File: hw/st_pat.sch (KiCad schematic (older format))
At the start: 16 parts

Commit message: Switch to use Feather M0 Adalogger board
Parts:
- removed C? (x2): 1uF, symbol Device:C_Small
- removed C?: 10uF, symbol Device:C_Small
- removed D?: LED, symbol Device:LED
- removed D?: MBR120, symbol Device:D
- removed J?: USB_B, symbol Connector:USB_B
- removed J?: BATTERY, symbol Connector:Conn_01x02_Female
- removed J?: Micro_SD_Card, symbol Connector:Micro_SD_Card
- removed Q?: DMG3415U, Package_TO_SOT_SMD:SOT-23, symbol Transistor_FET:DMG3414U
- removed R?: 10K, symbol Device:R_US
- removed R?: 1K, symbol Device:R_US
- removed R?: 100K, symbol Device:R_US
- removed U?: ATSAMD51J19A-A, Package_QFP:TQFP-64_10x10mm_P0.5mm, symbol MCU_Microchip_SAMD:ATSAMD51J19A-A
- removed U?: MCP73831-2-OT, Package_TO_SOT_SMD:SOT-23-5, symbol Battery_Management:MCP73831-2-OT
- removed U?: AP2112K-3.3, Package_TO_SOT_SMD:SOT-23-5, symbol Regulator_Linear:AP2112K-3.3
- added J1: Feather Left, symbol Connector:Conn_01x16_Female
- added J2: Feather Right, symbol Connector:Conn_01x12_Female
- added J3: Conn_01x09_Female, symbol Connector:Conn_01x09_Female
- added J4: BATTERY, symbol Connector:Conn_01x02_Female
- added SW1: SW_MEC_5G, symbol Switch:SW_MEC_5G
- gave numbers to parts that had none: 1
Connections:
- net labels added: +3V3, A0, A1, A2, A3, A4, A5, AREF, D10, D11, D12, D13, D5, D6, D7, D9, EN, MISO, MOSI, RST, RX, SCI, SCK, SDA, TX, VBAT
- net labels removed: +3.3V, D+, D-, SCLK, SD_CS, SD_MISO, SD_MOSI
- wire segments 33 -> 13
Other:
- note added: "FEATHER PINS"
- note added: "SHARP DISPLAY"
- note removed: "10K = 100mA\nMay change depending on battery"
- note removed: "I have no idea what capacitor values to use :P"
- moved on the sheet: U1

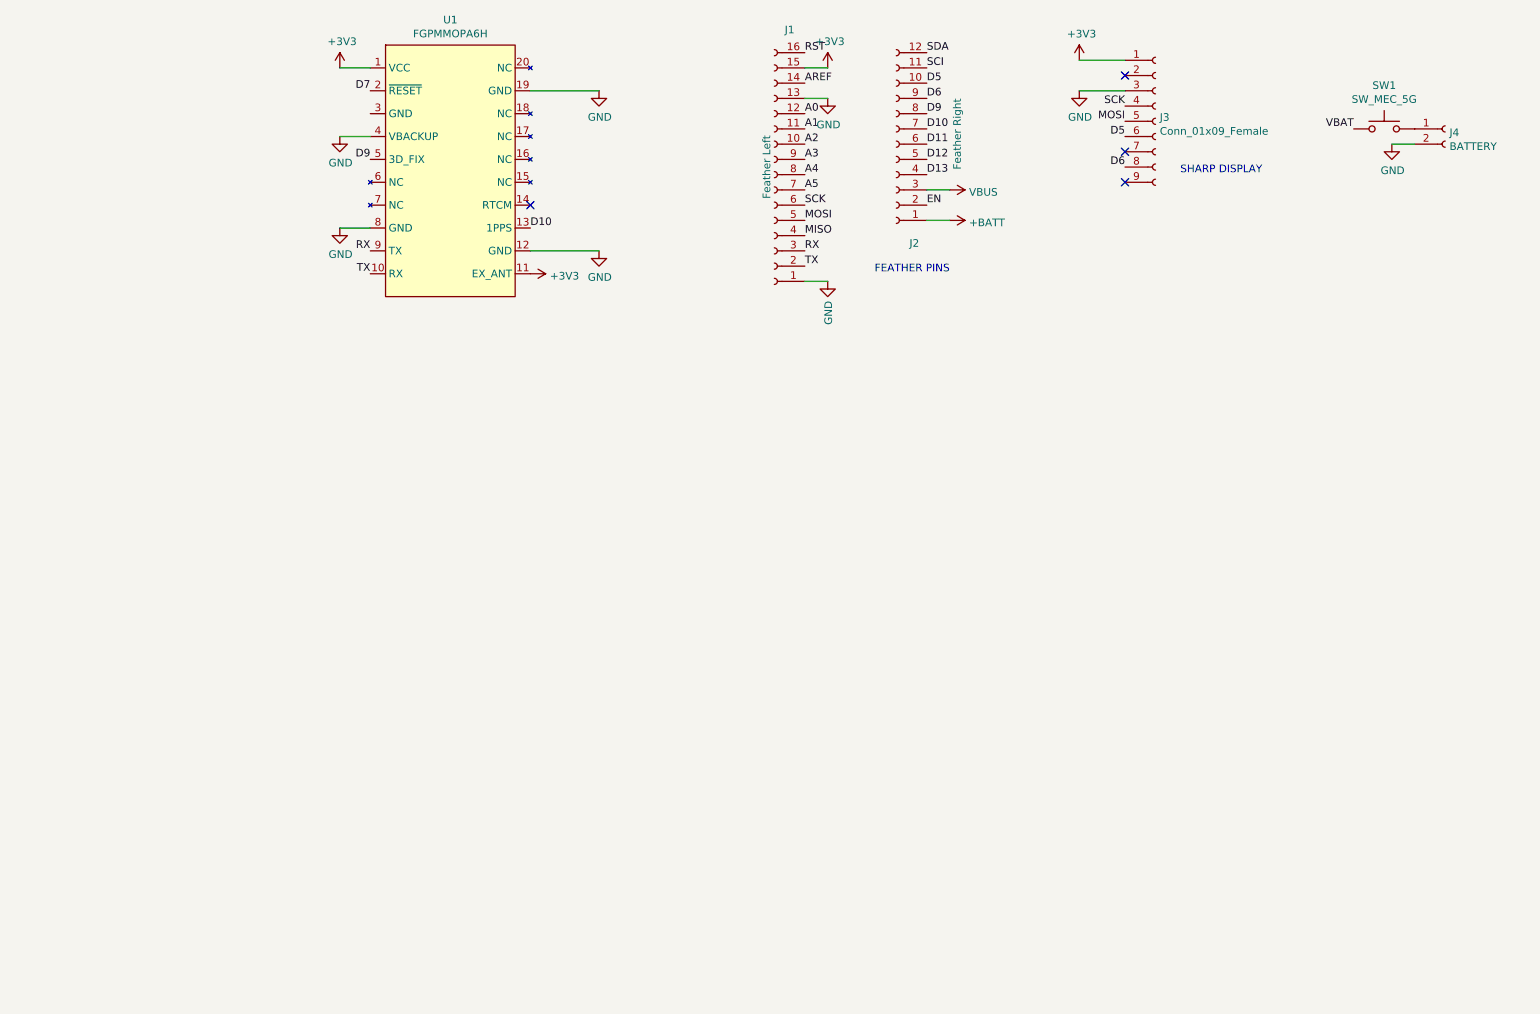
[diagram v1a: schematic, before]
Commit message: add compass to schematic
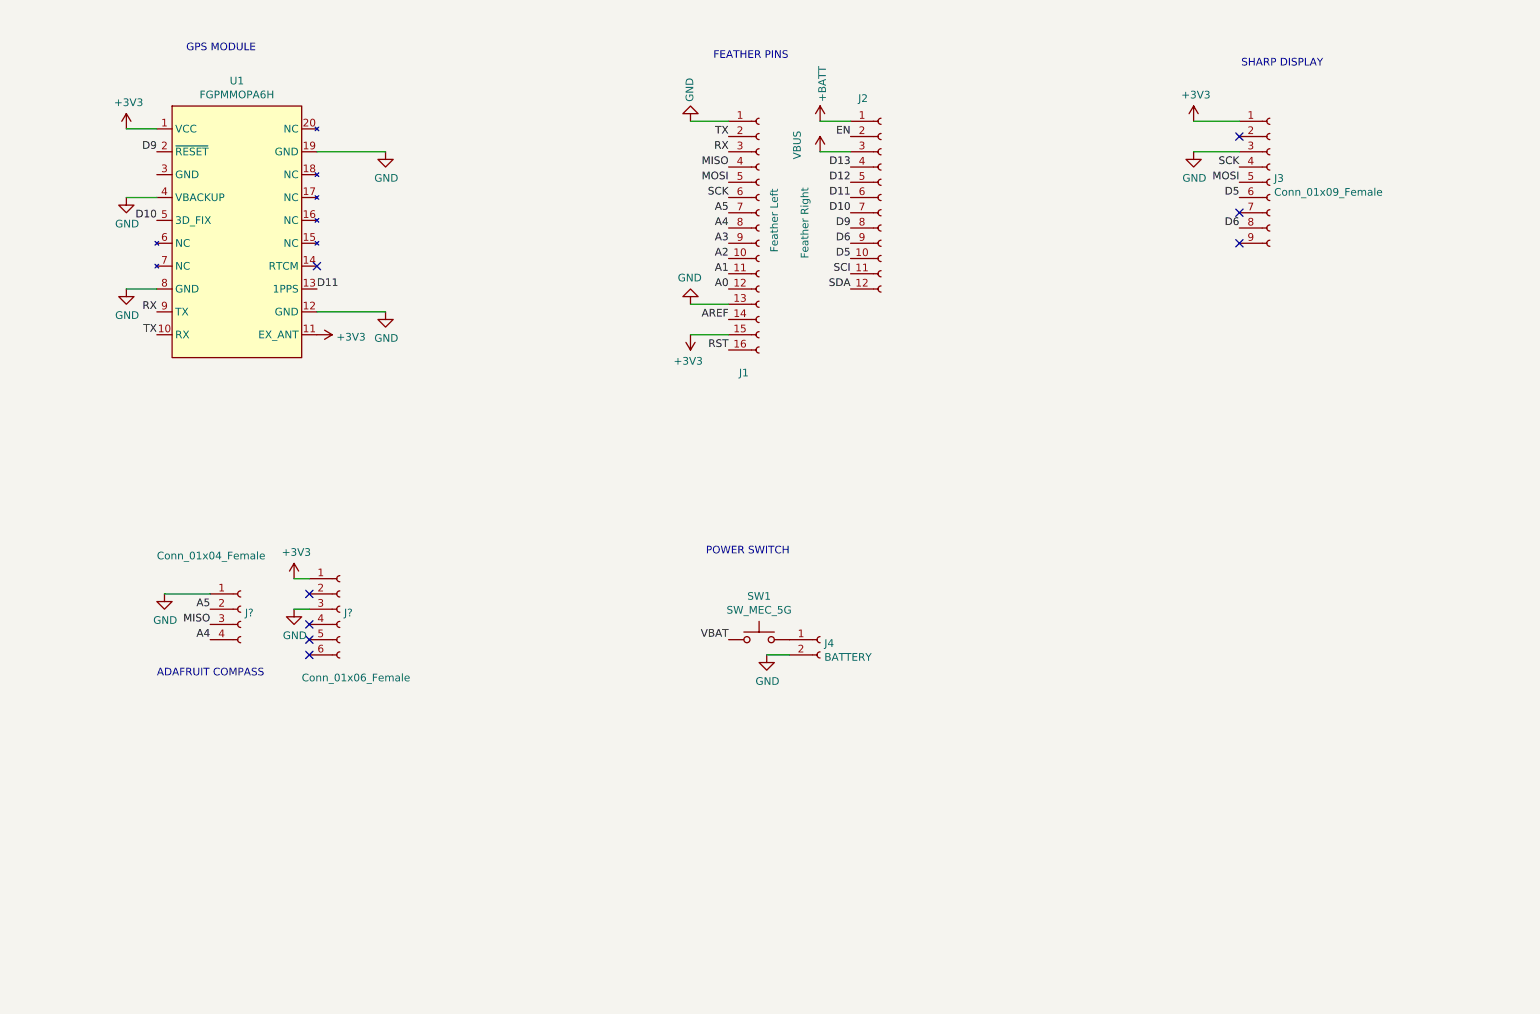
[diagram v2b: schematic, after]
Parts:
- added J?: Conn_01x04_Female, symbol Connector:Conn_01x04_Female
- added J?: Conn_01x06_Female, symbol Connector:Conn_01x06_Female
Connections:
- net D7 is gone; now on net D9: U1.2 (~RESET)
- net +3V3: now also J?.1 (Pin_1)
- net A4: now also J?.4 (Pin_4)
- net A5: now also J?.2 (Pin_2)
- net D10: now also U1.5 (3D_FIX); no longer U1.13 (1PPS)
- net D11: now also U1.13 (1PPS)
- net D9: no longer U1.5 (3D_FIX)
- net GND: now also J?.1 (Pin_1), J?.3 (Pin_3)
- net MISO: now also J?.3 (Pin_3)
- no-connect marks 4 -> 8
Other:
- note added: "ADAFRUIT COMPASS"
- note added: "GPS MODULE"
- note added: "POWER SWITCH"
- moved on the sheet: J1, J2, J3, J4, SW1, U1

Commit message: Update schematic - clearer label, add capacitor to GPS
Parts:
- added C1: 1uF, symbol Device:C_Small
- added C2: 0.01uF, symbol Device:C_Small
- added D1: LED, symbol Device:LED
- added R1: 330, symbol Device:R_US
- SW1: symbol Switch:SW_MEC_5G -> Switch:SW_SPST
- gave numbers to parts that had none: 2
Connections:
- net +3V3: now also C1.1, C2.1; no longer U1.11 (EX_ANT)
- net +BATT: now also SW1.1 (A)
- net GND: now also U1.3 (GND), C1.2, C2.2, R1.2; no longer U1.4 (VBACKUP)
- net SCK: now also J6.4 (Pin_4)
- net A4 renamed CPS_CS
- net A5 renamed CPS_RDY
- net D10 renamed GPS_FIX
- net GPS_FIX: now also D1.2 (A)
- net D11 renamed GPS_PPS
- net D5 renamed SHARP_CS
- net D6 renamed SHARP_DISP
- net D9 renamed GPS_RST
- net VBAT: no longer names the net of SW1.2 (B)
- net VBAT: now also J4.1 (Pin_1); no longer SW1.1 (A)
- new net: D1.1 (K), R1.1
- no-connect marks 8 -> 9
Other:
- moved on the sheet: J2, J6

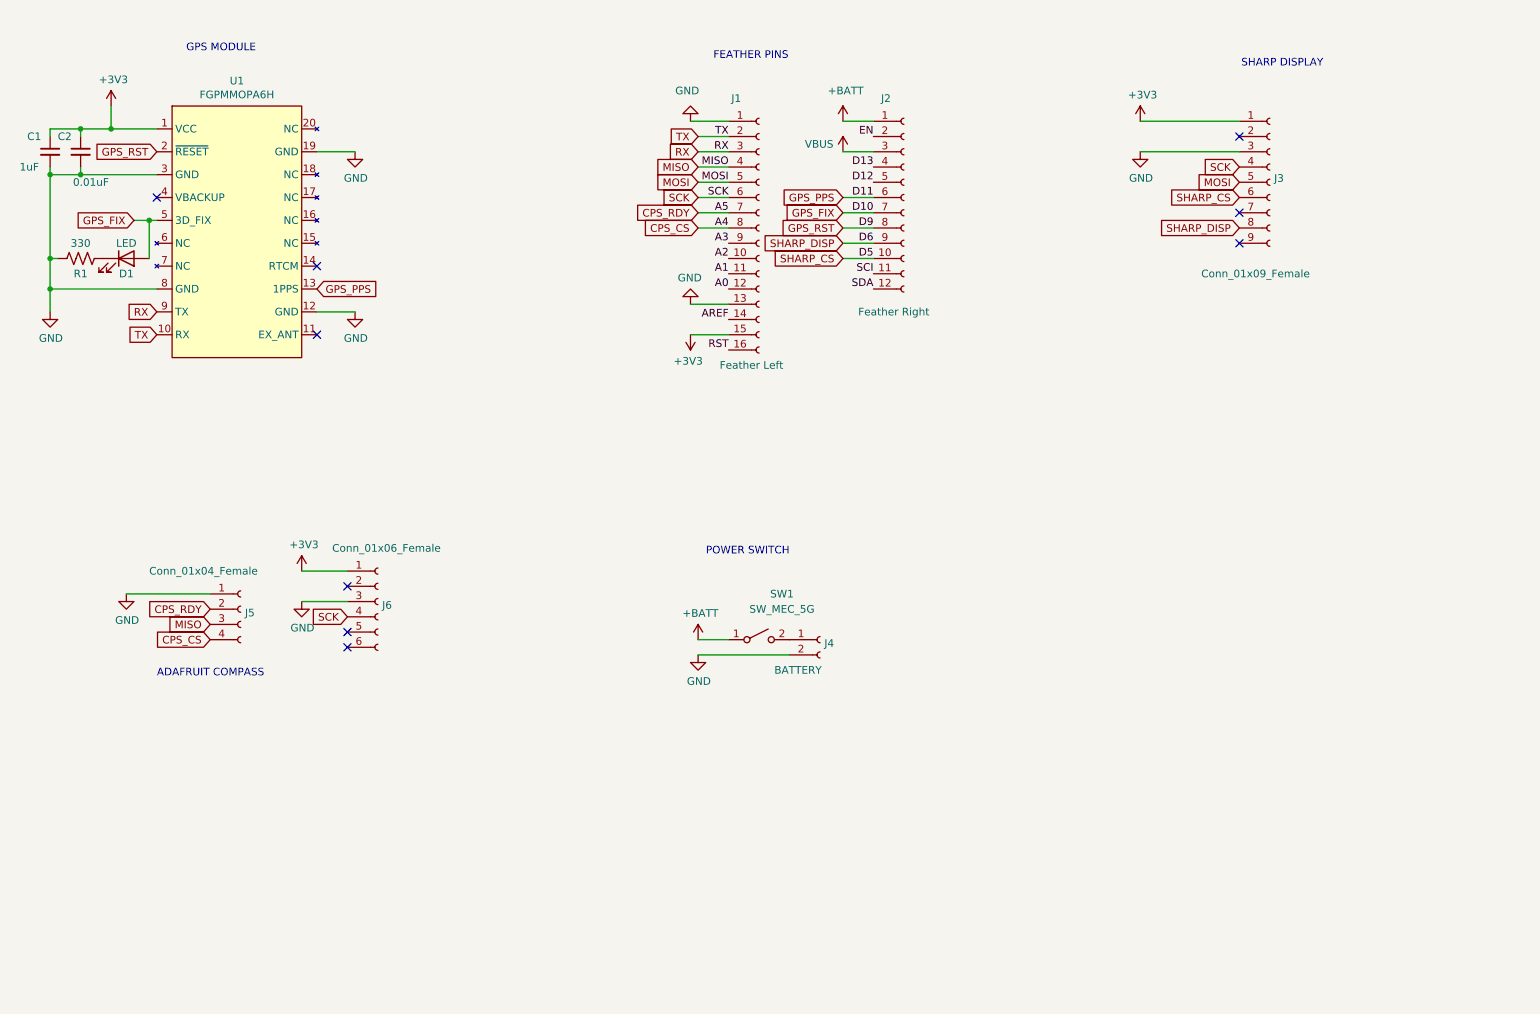
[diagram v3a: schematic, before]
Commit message: Remove global tags and fix ERC
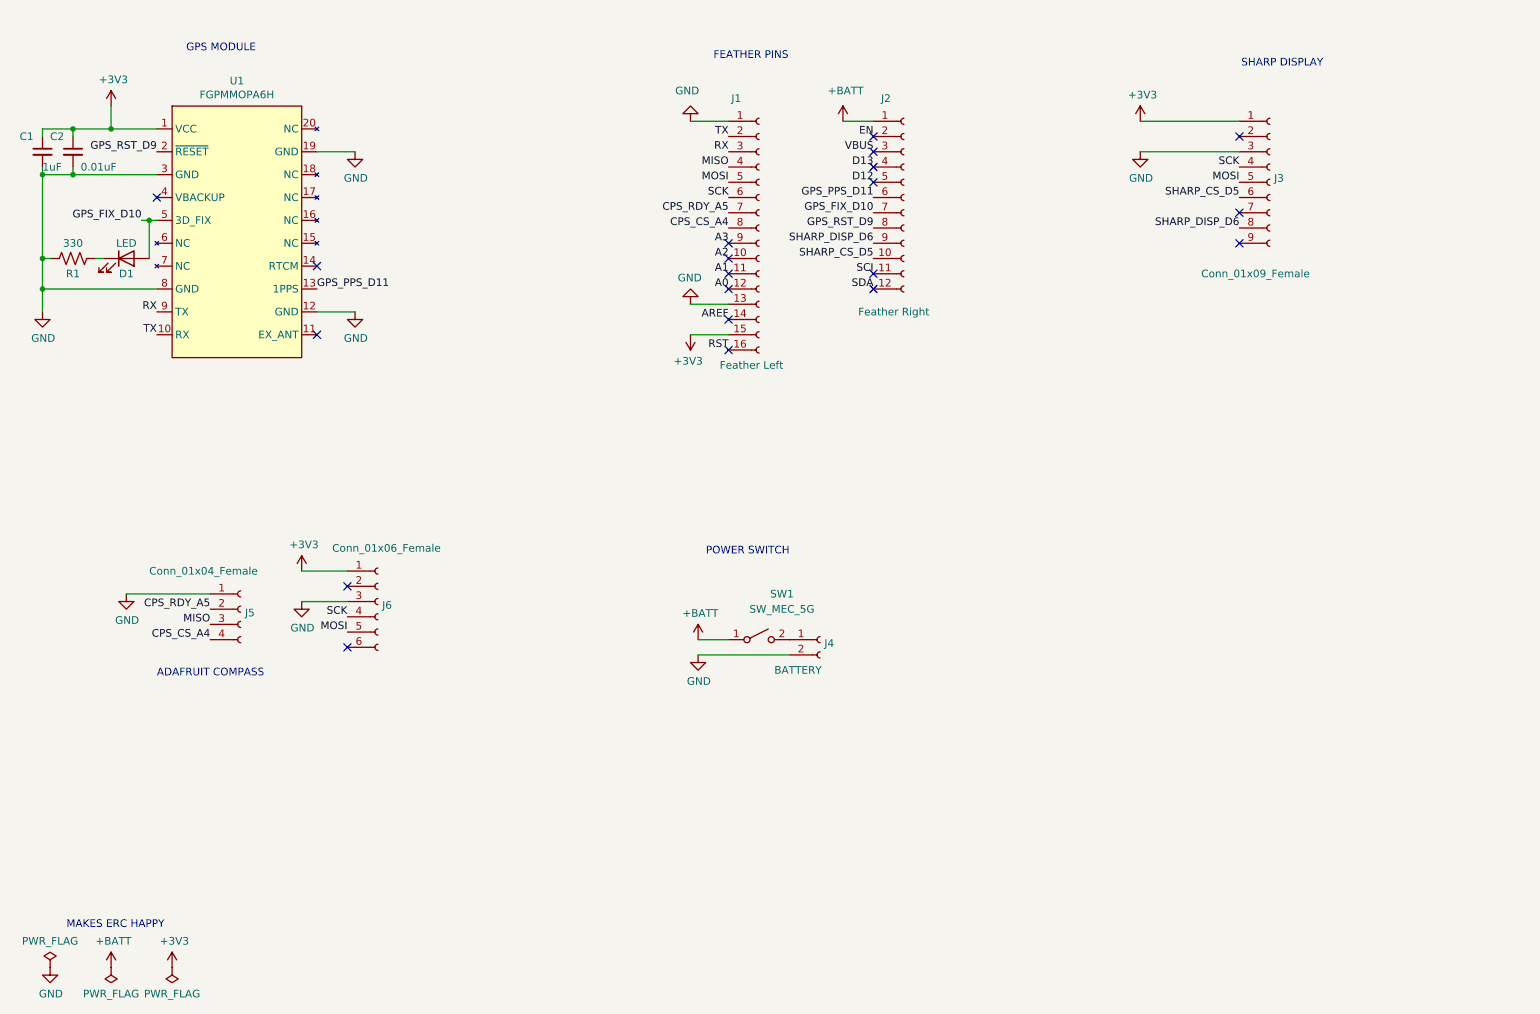
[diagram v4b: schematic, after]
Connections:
- net MOSI: now also J6.5 (Pin_5)
- net CPS_CS renamed CPS_CS_A4
- net CPS_RDY renamed CPS_RDY_A5
- net GPS_FIX renamed GPS_FIX_D10
- net GPS_PPS renamed GPS_PPS_D11
- net GPS_RST renamed GPS_RST_D9
- net SHARP_CS renamed SHARP_CS_D5
- net SHARP_DISP renamed SHARP_DISP_D6
- no-connect marks 9 -> 20
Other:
- note added: "MAKES ERC HAPPY"
- moved on the sheet: C1, C2, R1

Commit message: Add some leds and switches
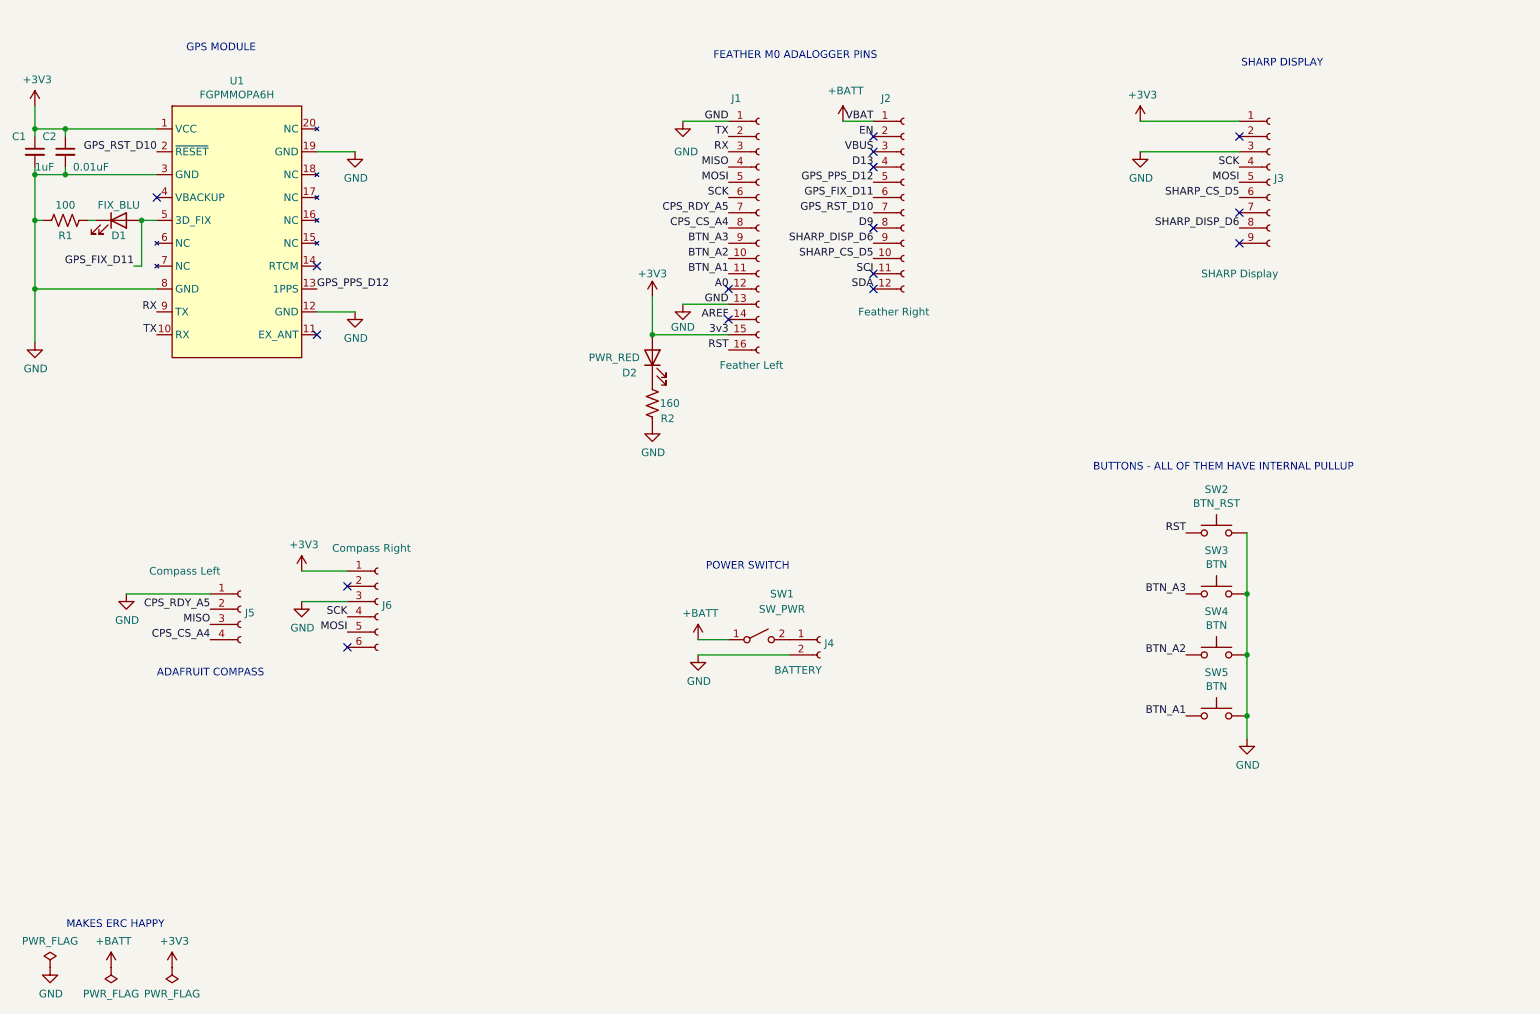
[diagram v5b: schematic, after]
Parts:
- added D2: PWR_RED, symbol Device:LED
- added R2: 160, symbol Device:R_US
- added SW2: BTN_RST, symbol Switch:SW_Push
- added SW3, SW4, SW5: BTN, symbol Switch:SW_Push
- D1: value LED -> FIX_BLU
- J3: value Conn_01x09_Female -> SHARP Display
- J5: value Conn_01x04_Female -> Compass Left
- J6: value Conn_01x06_Female -> Compass Right
- R1: value 330 -> 100
- SW1: value SW_MEC_5G -> SW_PWR
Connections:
- net +3V3: now also D2.2 (A)
- net GND: now also R2.1, SW2.2, SW3.2, SW4.2, SW5.2
- net RST: now also SW2.1
- net A1 renamed BTN_A1
- net BTN_A1: now also SW5.1
- net A2 renamed BTN_A2
- net BTN_A2: now also SW4.1
- net A3 renamed BTN_A3
- net BTN_A3: now also SW3.1
- net D12 renamed GPS_PPS_D12
- net GPS_PPS_D12: now also U1.13 (1PPS)
- net GPS_FIX_D10 renamed GPS_FIX_D11
- net GPS_FIX_D11: now also J2.6 (Pin_6); no longer J2.7 (Pin_7)
- removed net GPS_PPS_D11: J2.6 (Pin_6), U1.13 (1PPS)
- net GPS_RST_D9 renamed D9
- net D9: no longer U1.2 (~RESET)
- new net: D2.1 (K), R2.2
- new net GPS_RST_D10: J2.7 (Pin_7), U1.2 (~RESET)
- no-connect marks 20 -> 16
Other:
- note added: "BUTTONS - ALL OF THEM HAVE INTERNAL PULLUP"
- note added: "FEATHER M0 ADALOGGER PINS"
- note removed: "FEATHER PINS"
- moved on the sheet: C1, C2, D1, R1
